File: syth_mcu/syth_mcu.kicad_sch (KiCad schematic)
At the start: 31 parts, among them J10 Conn_01x20, J11 Conn_01x20, J4 Conn_01x04, J5 Conn_01x20, J6 Conn_01x20, J7 Conn_01x16, J8 Conn_01x08, SW1 SW_Push, SW10 Solder, SW11 SW_DIP_x03, SW13 Solder, SW2 SW_Push, SW3 SW_Push, SW4 SW_Push, SW5 SW_Push, SW6 SW_Push, SW7 SS12D10, SW8 Solder, SW9 Solder, U2 YAAJ_WeAct_BlackPill_Part_Like, U5 TFT_320x240

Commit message: Most routing, models for switch and fuses
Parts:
- added MCU5VFuse1: RXEF040, synth:RXEF040, symbol Device:Polyfuse
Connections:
- net D_5V: now also LeftConn1.8 (Pin_8), RightConn1.8 (Pin_8), MCU5VFuse1.1; no longer LeftConn1.4 (Pin_4), RightConn1.4 (Pin_4), SW7.2 (B)
- net GND: now also LeftConn1.4 (Pin_4), RightConn1.4 (Pin_4); no longer LeftConn1.8 (Pin_8), RightConn1.8 (Pin_8)
- net PB6: now also LeftConn1.6 (Pin_6), RightConn1.6 (Pin_6); no longer LeftConn1.7 (Pin_7), RightConn1.7 (Pin_7)
- net PB7: now also LeftConn1.5 (Pin_5), RightConn1.5 (Pin_5); no longer LeftConn1.6 (Pin_6), RightConn1.6 (Pin_6)
- net PC14: now also RightConn1.7 (Pin_7); no longer RightConn1.5 (Pin_5)
- net PC15: now also LeftConn1.7 (Pin_7); no longer LeftConn1.5 (Pin_5)
- new net: MCU5VFuse1.2, SW7.2 (B)
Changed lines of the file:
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@@
 	(wire
 		(pts
+			(xy 168.91 87.63) (xy 170.18 87.63)
+		)
+		(stroke
+			(width 0)
+			(type default)
+		)
+	)
+	(wire
+		(pts
 			(xy 82.55 95.25) (xy 82.55 81.28)
 		)
@@
 	(wire
 		(pts
+			(xy 160.02 87.63) (xy 161.29 87.63)
+		)
+		(stroke
+			(width 0)
+			(type default)
+		)
+	)
+	(wire
+		(pts
 			(xy 40.64 102.87) (xy 33.02 102.87)
 		)
@@
 	(global_label "PB7"
 		(shape input)
-		(at 134.62 80.01 0)
+		(at 134.62 82.55 0)
 		(fields_autoplaced yes)
 		(effects
@@
 		)
 		(property "Intersheetrefs" "${INTERSHEET_REFS}"
-			(at 141.3547 80.01 0)
+			(at 141.3547 82.55 0)
 			(hide yes)
 			(show_name no)
@@
 	(global_label "PB7"
 		(shape input)
-		(at 134.62 107.95 0)
+		(at 134.62 110.49 0)
 		(fields_autoplaced yes)
 		(effects
@@
 		)
 		(property "Intersheetrefs" "${INTERSHEET_REFS}"
-			(at 141.3547 107.95 0)
+			(at 141.3547 110.49 0)
 			(hide yes)
 			(show_name no)
@@
 	(global_label "D_5V"
 		(shape input)
-		(at 134.62 85.09 0)
+		(at 134.62 74.93 0)
 		(fields_autoplaced yes)
 		(effects
@@
 		)
 		(property "Intersheetrefs" "${INTERSHEET_REFS}"
-			(at 142.1409 85.09 0)
+			(at 142.1409 74.93 0)
 			(hide yes)
 			(show_name no)
@@
 	(global_label "PB6"
 		(shape input)
-		(at 134.62 105.41 0)
+		(at 134.62 107.95 0)
 		(fields_autoplaced yes)
 		(effects
@@
 		)
 		(property "Intersheetrefs" "${INTERSHEET_REFS}"
-			(at 141.3547 105.41 0)
+			(at 141.3547 107.95 0)
 			(hide yes)
 			(show_name no)
@@
 	(global_label "PC14"
 		(shape input)
-		(at 134.62 110.49 0)
+		(at 134.62 105.41 0)
 		(fields_autoplaced yes)
 		(effects
@@
 		)
 		(property "Intersheetrefs" "${INTERSHEET_REFS}"
-			(at 142.5642 110.49 0)
+			(at 142.5642 105.41 0)
 			(hide yes)
 			(show_name no)
@@
 	(global_label "PC15"
 		(shape input)
-		(at 134.62 82.55 0)
+		(at 134.62 77.47 0)
 		(fields_autoplaced yes)
 		(effects
@@
 		)
 		(property "Intersheetrefs" "${INTERSHEET_REFS}"
-			(at 142.5642 82.55 0)
+			(at 142.5642 77.47 0)
 			(hide yes)
 			(show_name no)
@@
 	(global_label "PB6"
 		(shape input)
-		(at 134.62 77.47 0)
+		(at 134.62 80.01 0)
 		(fields_autoplaced yes)
 		(effects
@@
 		)
 		(property "Intersheetrefs" "${INTERSHEET_REFS}"
-			(at 141.3547 77.47 0)
+			(at 141.3547 80.01 0)
 			(hide yes)
 			(show_name no)
@@
 	(global_label "D_5V"
 		(shape input)
-		(at 134.62 113.03 0)
+		(at 134.62 102.87 0)
 		(fields_autoplaced yes)
 		(effects
@@
 		)
 		(property "Intersheetrefs" "${INTERSHEET_REFS}"
-			(at 142.1409 113.03 0)
+			(at 142.1409 102.87 0)
 			(hide yes)
 			(show_name no)
@@
 	(global_label "D_5V"
 		(shape input)
-		(at 170.18 87.63 180)
+		(at 160.02 87.63 180)
 		(fields_autoplaced yes)
 		(effects
@@
 		)
 		(property "Intersheetrefs" "${INTERSHEET_REFS}"
-			(at 162.6591 87.63 0)
+			(at 152.4991 87.63 0)
 			(hide yes)
 			(show_name no)
@@
 	)
 	(symbol
+		(lib_id "Device:Polyfuse")
+		(at 165.1 87.63 90)
+		(unit 1)
+		(body_style 1)
+		(exclude_from_sim no)
+		(in_bom yes)
+		(on_board yes)
+		(in_pos_files yes)
+		(dnp no)
+		(fields_autoplaced yes)
+		(property "Reference" "MCU5VFuse1"
+			(at 165.1 81.28 90)
+			(show_name no)
+			(do_not_autoplace no)
+			(effects
+				(font
+					(size 1.27 1.27)
+				)
+			)
+		)
+		(property "Value" "RXEF040"
+			(at 165.1 83.82 90)
+			(show_name no)
+			(do_not_autoplace no)
+			(effects
+				(font
+					(size 1.27 1.27)
+				)
+			)
+		)
+		(property "Footprint" "synth:RXEF040"
+			(at 170.18 86.36 0)
+			(hide yes)
+			(show_name no)
+			(do_not_autoplace no)
+			(effects
+				(font
+					(size 1.27 1.27)
+				)
+				(justify left)
+			)
+		)
+		(property "Datasheet" ""
+			(at 165.1 87.63 0)
+			(hide yes)
+			(show_name no)
+			(do_not_autoplace no)
+			(effects
+				(font
+					(size 1.27 1.27)
+				)
+			)
+		)
+		(property "Description" "Resettable fuse, polymeric positive temperature coefficient"
+			(at 165.1 87.63 0)
+			(hide yes)
+			(show_name no)
+			(do_not_autoplace no)
+			(effects
+				(font
+					(size 1.27 1.27)
+				)
+			)
+		)
+		(pin "2"
+		)
+		(pin "1"
+		)
+		(instances
+			(project "syth_mcu"
+				(path "/6f6073ad-48fd-4b64-b32f-c8e9bfc21ddc"
+					(reference "MCU5VFuse1")
+					(unit 1)
+				)
+			)
+		)
+	)
+	(symbol
 		(lib_id "Switch:SW_SPST")
 		(at 58.42 129.54 270)
@@
 	(symbol
 		(lib_id "power:GND")
-		(at 134.62 74.93 90)
+		(at 134.62 85.09 90)
 		(unit 1)
 		(body_style 1)
@@
 		(fields_autoplaced yes)
 		(property "Reference" "#PWR07"
-			(at 140.97 74.93 0)
+			(at 140.97 85.09 0)
 			(hide yes)
 			(show_name no)
@@
 		)
 		(property "Value" "GND"
-			(at 138.43 74.9301 90)
+			(at 138.43 85.0901 90)
 			(show_name no)
 			(do_not_autoplace no)
@@
 		)
 		(property "Footprint" ""
-			(at 134.62 74.93 0)
+			(at 134.62 85.09 0)
 			(hide yes)
 			(show_name no)
@@
 		)
 		(property "Datasheet" ""
-			(at 134.62 74.93 0)
+			(at 134.62 85.09 0)
 			(hide yes)
 			(show_name no)
@@
 		)
 		(property "Description" "Power symbol creates a global label with name \"GND\" , ground"
-			(at 134.62 74.93 0)
+			(at 134.62 85.09 0)
 			(hide yes)
 			(show_name no)
@@
 	(symbol
 		(lib_id "power:GND")
-		(at 134.62 102.87 90)
+		(at 134.62 113.03 90)
 		(unit 1)
 		(body_style 1)
@@
 		(fields_autoplaced yes)
 		(property "Reference" "#PWR08"
-			(at 140.97 102.87 0)
+			(at 140.97 113.03 0)
 			(hide yes)
 			(show_name no)
@@
 		)
 		(property "Value" "GND"
-			(at 138.43 102.8701 90)
+			(at 138.43 113.0301 90)
 			(show_name no)
 			(do_not_autoplace no)
@@
 		)
 		(property "Footprint" ""
-			(at 134.62 102.87 0)
+			(at 134.62 113.03 0)
 			(hide yes)
 			(show_name no)
@@
 		)
 		(property "Datasheet" ""
-			(at 134.62 102.87 0)
+			(at 134.62 113.03 0)
 			(hide yes)
 			(show_name no)
@@
 		)
 		(property "Description" "Power symbol creates a global label with name \"GND\" , ground"
-			(at 134.62 102.87 0)
+			(at 134.62 113.03 0)
 			(hide yes)
 			(show_name no)

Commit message: System check, DRC runs
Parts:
- added C6: 1uF, symbol Device:C
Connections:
- net AMS2_3.3V: now also C6.2
- net GND: now also C6.1
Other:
- note added: "0.20mm GPIO traces short with 0.80A peak at (30+60)deg"
- moved on the sheet: J8
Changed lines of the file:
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@@
 	(text "ENN\n"
 		(exclude_from_sim no)
-		(at 72.39 85.344 0)
+		(at 83.82 85.344 0)
 		(effects
 			(font
@@
 		)
 	)
+	(text "0.20mm GPIO traces short with 0.80A peak\nat (30+60)deg "
+		(exclude_from_sim no)
+		(at 207.01 88.138 0)
+		(effects
+			(font
+				(size 1.016 1.016)
+			)
+			(justify left)
+		)
+	)
 	(junction
 		(at 176.53 60.96)
@@
 	(wire
 		(pts
-			(xy 85.09 81.28) (xy 85.09 95.25)
+			(xy 96.52 81.28) (xy 96.52 95.25)
 		)
 		(stroke
@@
 	(wire
 		(pts
-			(xy 69.85 81.28) (xy 69.85 95.25)
+			(xy 81.28 81.28) (xy 81.28 92.71)
 		)
 		(stroke
@@
 	(wire
 		(pts
-			(xy 80.01 81.28) (xy 80.01 95.25)
+			(xy 91.44 81.28) (xy 91.44 95.25)
 		)
 		(stroke
@@
 	(wire
 		(pts
-			(xy 74.93 95.25) (xy 74.93 81.28)
+			(xy 86.36 95.25) (xy 86.36 81.28)
 		)
 		(stroke
@@
 	(wire
 		(pts
+			(xy 78.74 82.55) (xy 78.74 81.28)
+		)
+		(stroke
+			(width 0)
+			(type default)
+		)
+	)
+	(wire
+		(pts
 			(xy 40.64 107.95) (xy 33.02 107.95)
 		)
@@
 	(wire
 		(pts
-			(xy 82.55 95.25) (xy 82.55 81.28)
+			(xy 93.98 95.25) (xy 93.98 81.28)
 		)
 		(stroke
@@
 	(wire
 		(pts
+			(xy 73.66 82.55) (xy 78.74 82.55)
+		)
+		(stroke
+			(width 0)
+			(type default)
+		)
+	)
+	(wire
+		(pts
 			(xy 207.01 69.85) (xy 210.82 69.85)
 		)
@@
 	(wire
 		(pts
+			(xy 73.66 92.71) (xy 73.66 82.55)
+		)
+		(stroke
+			(width 0)
+			(type default)
+		)
+	)
+	(wire
+		(pts
 			(xy 58.42 123.19) (xy 58.42 124.46)
 		)
@@
 	(wire
 		(pts
-			(xy 72.39 83.82) (xy 72.39 81.28)
+			(xy 83.82 83.82) (xy 83.82 81.28)
 		)
 		(stroke
@@
 	(wire
 		(pts
-			(xy 77.47 81.28) (xy 77.47 95.25)
+			(xy 88.9 81.28) (xy 88.9 95.25)
 		)
 		(stroke
@@
 	(global_label "AMS2_3.3V"
 		(shape input)
-		(at 69.85 95.25 270)
+		(at 81.28 92.71 270)
 		(fields_autoplaced yes)
 		(effects
@@
 		)
 		(property "Intersheetrefs" "${INTERSHEET_REFS}"
-			(at 69.85 108.2742 90)
+			(at 81.28 105.7342 90)
 			(hide yes)
 			(show_name no)
@@
 	(global_label "S1"
 		(shape input)
-		(at 77.47 95.25 270)
+		(at 88.9 95.25 270)
 		(fields_autoplaced yes)
 		(effects
@@
 		)
 		(property "Intersheetrefs" "${INTERSHEET_REFS}"
-			(at 77.47 100.6542 90)
+			(at 88.9 100.6542 90)
 			(hide yes)
 			(show_name no)
@@
 	(global_label "S0"
 		(shape input)
-		(at 74.93 95.25 270)
+		(at 86.36 95.25 270)
 		(fields_autoplaced yes)
 		(effects
@@
 		)
 		(property "Intersheetrefs" "${INTERSHEET_REFS}"
-			(at 74.93 100.6542 90)
+			(at 86.36 100.6542 90)
 			(hide yes)
 			(show_name no)
@@
 	(global_label "PA2"
 		(shape input)
-		(at 80.01 88.9 0)
+		(at 91.44 88.9 0)
 		(fields_autoplaced yes)
 		(effects
@@
 		)
 		(property "Intersheetrefs" "${INTERSHEET_REFS}"
-			(at 86.5633 88.9 0)
+			(at 97.9933 88.9 0)
 			(hide yes)
 			(show_name no)
@@
 	(global_label "GND"
 		(shape input)
-		(at 67.31 81.28 270)
+		(at 73.66 92.71 270)
 		(fields_autoplaced yes)
 		(effects
@@
 		)
 		(property "Intersheetrefs" "${INTERSHEET_REFS}"
-			(at 67.31 88.1357 90)
+			(at 73.66 99.5657 90)
 			(hide yes)
 			(show_name no)
@@
 	(global_label "S3"
 		(shape input)
-		(at 82.55 95.25 270)
+		(at 93.98 95.25 270)
 		(fields_autoplaced yes)
 		(effects
@@
 		)
 		(property "Intersheetrefs" "${INTERSHEET_REFS}"
-			(at 82.55 100.6542 90)
+			(at 93.98 100.6542 90)
 			(hide yes)
 			(show_name no)
@@
 	(global_label "SIG"
 		(shape input)
-		(at 85.09 95.25 270)
+		(at 96.52 95.25 270)
 		(fields_autoplaced yes)
 		(effects
@@
 		)
 		(property "Intersheetrefs" "${INTERSHEET_REFS}"
-			(at 85.09 101.3195 90)
+			(at 96.52 101.3195 90)
 			(hide yes)
 			(show_name no)
@@
 	(global_label "PA1"
 		(shape input)
-		(at 77.47 91.44 0)
+		(at 88.9 91.44 0)
 		(fields_autoplaced yes)
 		(effects
@@
 		)
 		(property "Intersheetrefs" "${INTERSHEET_REFS}"
-			(at 84.0233 91.44 0)
+			(at 95.4533 91.44 0)
 			(hide yes)
 			(show_name no)
@@
 	(global_label "PA0"
 		(shape input)
-		(at 74.93 93.98 0)
+		(at 86.36 93.98 0)
 		(fields_autoplaced yes)
 		(effects
@@
 		)
 		(property "Intersheetrefs" "${INTERSHEET_REFS}"
-			(at 81.4833 93.98 0)
+			(at 92.9133 93.98 0)
 			(hide yes)
 			(show_name no)
@@
 	(global_label "S2"
 		(shape input)
-		(at 80.01 95.25 270)
+		(at 91.44 95.25 270)
 		(fields_autoplaced yes)
 		(effects
@@
 		)
 		(property "Intersheetrefs" "${INTERSHEET_REFS}"
-			(at 80.01 100.6542 90)
+			(at 91.44 100.6542 90)
 			(hide yes)
 			(show_name no)
@@
 	(global_label "PA3"
 		(shape input)
-		(at 82.55 86.36 0)
+		(at 93.98 86.36 0)
 		(fields_autoplaced yes)
 		(effects
@@
 		)
 		(property "Intersheetrefs" "${INTERSHEET_REFS}"
-			(at 89.1033 86.36 0)
+			(at 100.5333 86.36 0)
 			(hide yes)
 			(show_name no)
@@
 	(global_label "PA4"
 		(shape input)
-		(at 85.09 83.82 0)
+		(at 96.52 83.82 0)
 		(fields_autoplaced yes)
 		(effects
@@
 		)
 		(property "Intersheetrefs" "${INTERSHEET_REFS}"
-			(at 91.6433 83.82 0)
+			(at 103.0733 83.82 0)
 			(hide yes)
 			(show_name no)
@@
 	(global_label "GND"
 		(shape input)
-		(at 72.39 82.55 0)
+		(at 83.82 82.55 0)
 		(fields_autoplaced yes)
 		(effects
@@
 		)
 		(property "Intersheetrefs" "${INTERSHEET_REFS}"
-			(at 79.2457 82.55 0)
+			(at 90.6757 82.55 0)
 			(hide yes)
 			(show_name no)
@@
 	)
 	(symbol
+		(lib_id "Device:C")
+		(at 77.47 92.71 90)
+		(unit 1)
+		(body_style 1)
+		(exclude_from_sim no)
+		(in_bom yes)
+		(on_board yes)
+		(in_pos_files yes)
+		(dnp no)
+		(fields_autoplaced yes)
+		(property "Reference" "C6"
+			(at 77.47 85.09 90)
+			(show_name no)
+			(do_not_autoplace no)
+			(effects
+				(font
+					(size 1.27 1.27)
+				)
+			)
+		)
+		(property "Value" "1uF"
+			(at 77.47 87.63 90)
+			(show_name no)
+			(do_not_autoplace no)
+			(effects
+				(font
+					(size 1.27 1.27)
+				)
+			)
+		)
+		(property "Footprint" ""
+			(at 81.28 91.7448 0)
+			(hide yes)
+			(show_name no)
+			(do_not_autoplace no)
+			(effects
+				(font
+					(size 1.27 1.27)
+				)
+			)
+		)
+		(property "Datasheet" ""
+			(at 77.47 92.71 0)
+			(hide yes)
+			(show_name no)
+			(do_not_autoplace no)
+			(effects
+				(font
+					(size 1.27 1.27)
+				)
+			)
+		)
+		(property "Description" "Unpolarized capacitor"
+			(at 77.47 92.71 0)
+			(hide yes)
+			(show_name no)
+			(do_not_autoplace no)
+			(effects
+				(font
+					(size 1.27 1.27)
+				)
+			)
+		)
+		(pin "1"
+		)
+		(pin "2"
+		)
+		(instances
+			(project "syth_mcu"
+				(path "/6f6073ad-48fd-4b64-b32f-c8e9bfc21ddc"
+					(reference "C6")
+					(unit 1)
+				)
+			)
+		)
+	)
+	(symbol
 		(lib_id "Connector_Generic:Conn_01x20")
 		(at 83.82 38.1 0)
@@
 	(symbol
 		(lib_id "Connector_Generic:Conn_01x08")
-		(at 77.47 76.2 270)
+		(at 88.9 76.2 270)
 		(mirror x)
 		(unit 1)
@@
 		(dnp no)
 		(property "Reference" "J8"
-			(at 76.454 70.104 90)
+			(at 87.884 70.104 90)
 			(show_name no)
 			(do_not_autoplace no)
@@
 		)
 		(property "Value" "Conn_01x08"
-			(at 76.2 72.39 90)
+			(at 87.63 72.39 90)
 			(show_name no)
 			(do_not_autoplace no)
@@
 		)
 		(property "Footprint" "Connector_PinSocket_2.54mm:PinSocket_1x08_P2.54mm_Vertical"
-			(at 77.47 76.2 0)
+			(at 88.9 76.2 0)
 			(hide yes)
 			(show_name no)
@@
 		)
 		(property "Datasheet" ""
-			(at 77.47 76.2 0)
+			(at 88.9 76.2 0)
 			(hide yes)
 			(show_name no)
@@
 		)
 		(property "Description" "Generic connector, single row, 01x08, script generated (kicad-library-utils/schlib/autogen/connector/)"
-			(at 77.47 76.2 0)
+			(at 88.9 76.2 0)
 			(hide yes)
 			(show_name no)

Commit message: add screw, removed serial rev.pol diode
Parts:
- added H13, H14, H15: MountingHole, MountingHole:MountingHole_3.2mm_M3, symbol Mechanical:MountingHole
- C6: footprint (none) -> Capacitor_THT:C_Disc_D5.0mm_W2.5mm_P5.00mm
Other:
- moved on the sheet: SW10, SW13, SW9

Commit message: pcb: switch footprint to Cherry MX hotswap, reroute traces
- Replace Kailh Choc V1 hotswap footprints with Cherry MX compatible footprints
- Adjust switch spacing and reroute affected traces for new footprint geometry
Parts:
- SW1, SW2, SW3, SW4, SW5, SW6: footprint Switch_Keyboard_Hotswap_Kailh:SW_Hotswap_Kailh_Choc_V1_1.00u -> Button_Switch_Keyboard:SW_Cherry_MX_1.00u_PCB
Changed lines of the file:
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@@
 			)
 		)
-		(property "Footprint" "Switch_Keyboard_Hotswap_Kailh:SW_Hotswap_Kailh_Choc_V1_1.00u"
+		(property "Footprint" "Button_Switch_Keyboard:SW_Cherry_MX_1.00u_PCB"
 			(at 99.06 179.07 0)
 			(hide yes)
@@
 			)
 		)
-		(property "Footprint" "Switch_Keyboard_Hotswap_Kailh:SW_Hotswap_Kailh_Choc_V1_1.00u"
+		(property "Footprint" "Button_Switch_Keyboard:SW_Cherry_MX_1.00u_PCB"
 			(at 41.91 179.07 0)
 			(hide yes)
@@
 			)
 		)
-		(property "Footprint" "Switch_Keyboard_Hotswap_Kailh:SW_Hotswap_Kailh_Choc_V1_1.00u"
+		(property "Footprint" "Button_Switch_Keyboard:SW_Cherry_MX_1.00u_PCB"
 			(at 71.12 179.07 0)
 			(hide yes)
@@
 			)
 		)
-		(property "Footprint" "Switch_Keyboard_Hotswap_Kailh:SW_Hotswap_Kailh_Choc_V1_1.00u"
+		(property "Footprint" "Button_Switch_Keyboard:SW_Cherry_MX_1.00u_PCB"
 			(at 26.67 179.07 0)
 			(hide yes)
@@
 			)
 		)
-		(property "Footprint" "Switch_Keyboard_Hotswap_Kailh:SW_Hotswap_Kailh_Choc_V1_1.00u"
+		(property "Footprint" "Button_Switch_Keyboard:SW_Cherry_MX_1.00u_PCB"
 			(at 57.15 179.07 0)
 			(hide yes)
@@
 			)
 		)
-		(property "Footprint" "Switch_Keyboard_Hotswap_Kailh:SW_Hotswap_Kailh_Choc_V1_1.00u"
+		(property "Footprint" "Button_Switch_Keyboard:SW_Cherry_MX_1.00u_PCB"
 			(at 85.09 179.07 0)
 			(hide yes)

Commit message: pcb: Gateron hotswap footprint (marbastlib KS-2P02) + route J4-J7 pins
- SW1-SW6: replace Cherry MX PCB solder footprint with
  PCM_marbastlib-mx:SW_MX_HS_KS-2P02B01-01_1u for hotswap socket support
- Route Net-(J4-Pin_1..4) connecting J4.1-4 to J7.13-16
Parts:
- SW1, SW2, SW3, SW4, SW5, SW6: footprint Button_Switch_Keyboard:SW_Cherry_MX_1.00u_PCB -> PCM_marbastlib-mx:SW_MX_HS_KS-2P02B01-01_1u
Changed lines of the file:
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@@
 			)
 		)
-		(property "Footprint" "Button_Switch_Keyboard:SW_Cherry_MX_1.00u_PCB"
+		(property "Footprint" "PCM_marbastlib-mx:SW_MX_HS_KS-2P02B01-01_1u"
 			(at 99.06 179.07 0)
 			(hide yes)
@@
 			)
 		)
-		(property "Footprint" "Button_Switch_Keyboard:SW_Cherry_MX_1.00u_PCB"
+		(property "Footprint" "PCM_marbastlib-mx:SW_MX_HS_KS-2P02B01-01_1u"
 			(at 41.91 179.07 0)
 			(hide yes)
@@
 			)
 		)
-		(property "Footprint" "Button_Switch_Keyboard:SW_Cherry_MX_1.00u_PCB"
+		(property "Footprint" "PCM_marbastlib-mx:SW_MX_HS_KS-2P02B01-01_1u"
 			(at 71.12 179.07 0)
 			(hide yes)
@@
 			)
 		)
-		(property "Footprint" "Button_Switch_Keyboard:SW_Cherry_MX_1.00u_PCB"
+		(property "Footprint" "PCM_marbastlib-mx:SW_MX_HS_KS-2P02B01-01_1u"
 			(at 26.67 179.07 0)
 			(hide yes)
@@
 			)
 		)
-		(property "Footprint" "Button_Switch_Keyboard:SW_Cherry_MX_1.00u_PCB"
+		(property "Footprint" "PCM_marbastlib-mx:SW_MX_HS_KS-2P02B01-01_1u"
 			(at 57.15 179.07 0)
 			(hide yes)
@@
 			)
 		)
-		(property "Footprint" "Button_Switch_Keyboard:SW_Cherry_MX_1.00u_PCB"
+		(property "Footprint" "PCM_marbastlib-mx:SW_MX_HS_KS-2P02B01-01_1u"
 			(at 85.09 179.07 0)
 			(hide yes)

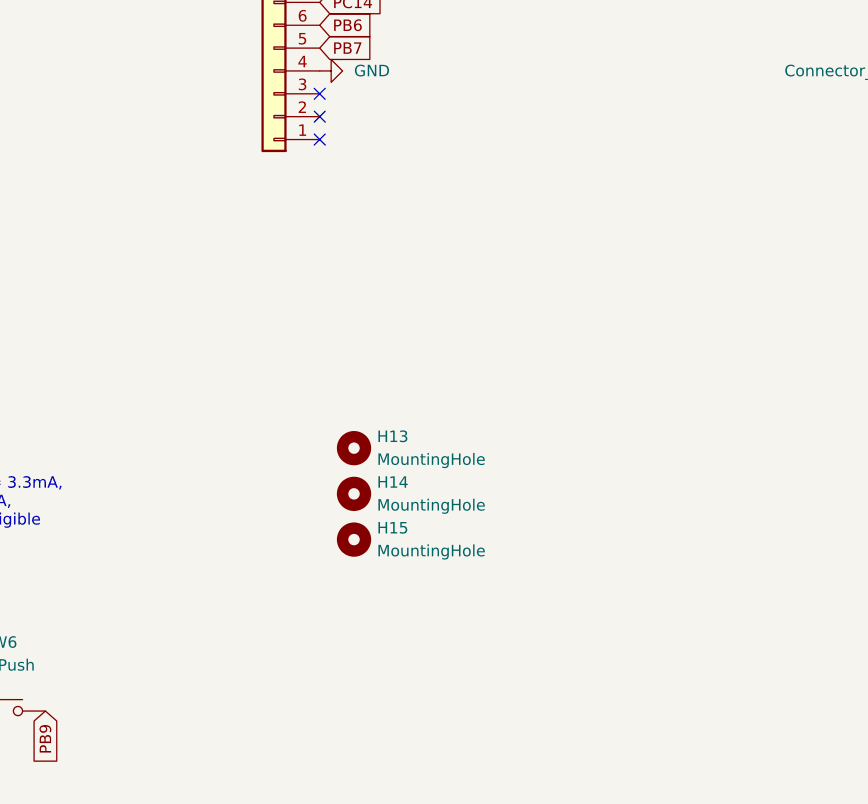
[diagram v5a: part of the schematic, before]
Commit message: Pogo with 2x05 side connectors
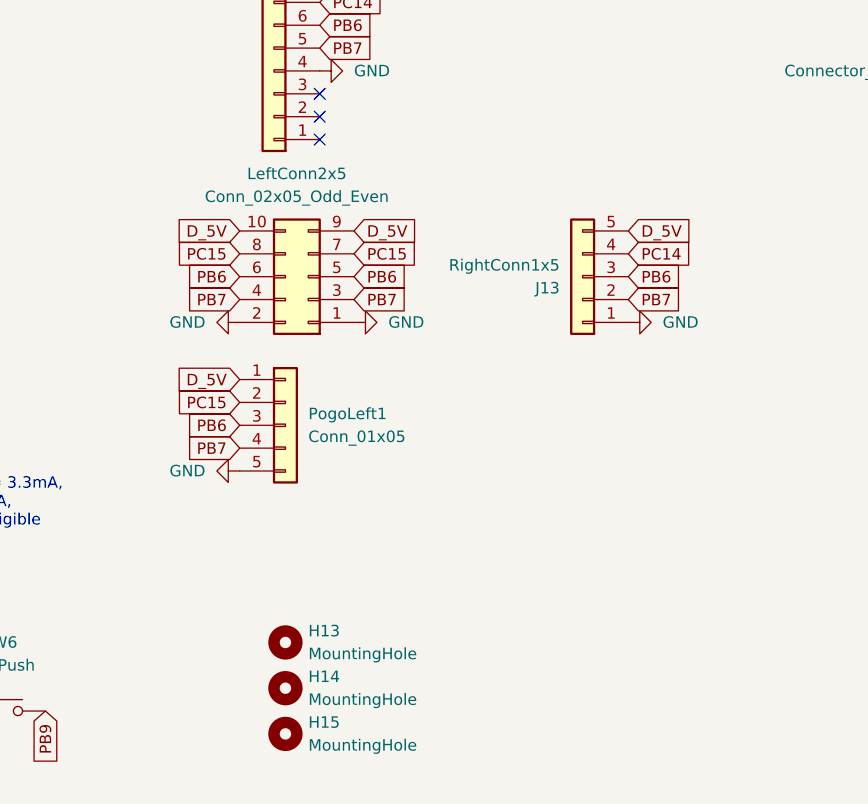
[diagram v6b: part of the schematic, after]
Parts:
- added J13: RightConn1x5, Connector_PinSocket_2.54mm:PinSocket_1x05_P2.54mm_Horizontal, symbol Connector_Generic:Conn_01x05
- added LeftConn2x5: Conn_02x05_Odd_Even, Connector_PinHeader_2.54mm:PinHeader_2x05_P2.54mm_Horizontal, symbol Connector_Generic:Conn_02x05_Odd_Even
- added PogoLeft1: Conn_01x05, synth:CONN-TH_PR5L4015-5P-C-F, symbol Connector_Generic:Conn_01x05
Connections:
- net D_5V: now also J13.5 (Pin_5), LeftConn2x5.10 (Pin_10), LeftConn2x5.9 (Pin_9), PogoLeft1.1 (Pin_1)
- net GND: now also J13.1 (Pin_1), LeftConn2x5.1 (Pin_1), LeftConn2x5.2 (Pin_2), PogoLeft1.5 (Pin_5)
- net PB6: now also J13.3 (Pin_3), LeftConn2x5.5 (Pin_5), LeftConn2x5.6 (Pin_6), PogoLeft1.3 (Pin_3)
- net PB7: now also J13.2 (Pin_2), LeftConn2x5.3 (Pin_3), LeftConn2x5.4 (Pin_4), PogoLeft1.4 (Pin_4)
- net PC14: now also J13.4 (Pin_4)
- net PC15: now also LeftConn2x5.7 (Pin_7), LeftConn2x5.8 (Pin_8), PogoLeft1.2 (Pin_2)
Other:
- moved on the sheet: H13, H14, H15
